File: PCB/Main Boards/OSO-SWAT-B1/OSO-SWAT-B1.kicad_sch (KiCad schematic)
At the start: 35 parts, among them J1 OSO_SWD, U1 ATSAML22J18A-MUT, U2 MIC5365-3.3YC5-TR, X1 32.768 kHz, 12.5 pF

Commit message: as sent to JLCPCB 10/12
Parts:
- C1: LCSC Part (none) -> C19702
- C2, C3, C4: LCSC Part (none) -> C14663
- C5, C6, C9: LCSC Part (none) -> C15849
- C7, C8: LCSC Part (none) -> C1555
- D1: LCSC Part (none) -> C2972951
- FID10, FID11, FID7, FID8, FID9: Field4 (none) -> ${REFERENCE}; now not fitted; now left out of the parts list
- J1, U$2: now left out of the parts list
- L1: LCSC Part (none) -> C139245
- LED0: LCSC Part (none) -> C5829791
- R1: value TBD -> 1K; LCSC Part (none) -> C21190
- R3: LCSC Part (none) -> C440252
- R4: LCSC Part (none) -> C95204
- R6: LCSC Part (none) -> C21190
- R7: LCSC Part (none) -> C22775
- RESET0, RESET1: LCSC Part (none) -> C5185477
- TP1, TP10, TP6, TP7, TP8, TP9: now not fitted; now left out of the parts list
- U1: LCSC Part (none) -> C618315
- U2: LCSC Part (none) -> C47945
- X1: Field4 (none) -> ${REFERENCE}; LCSC Part (none) -> C2613043

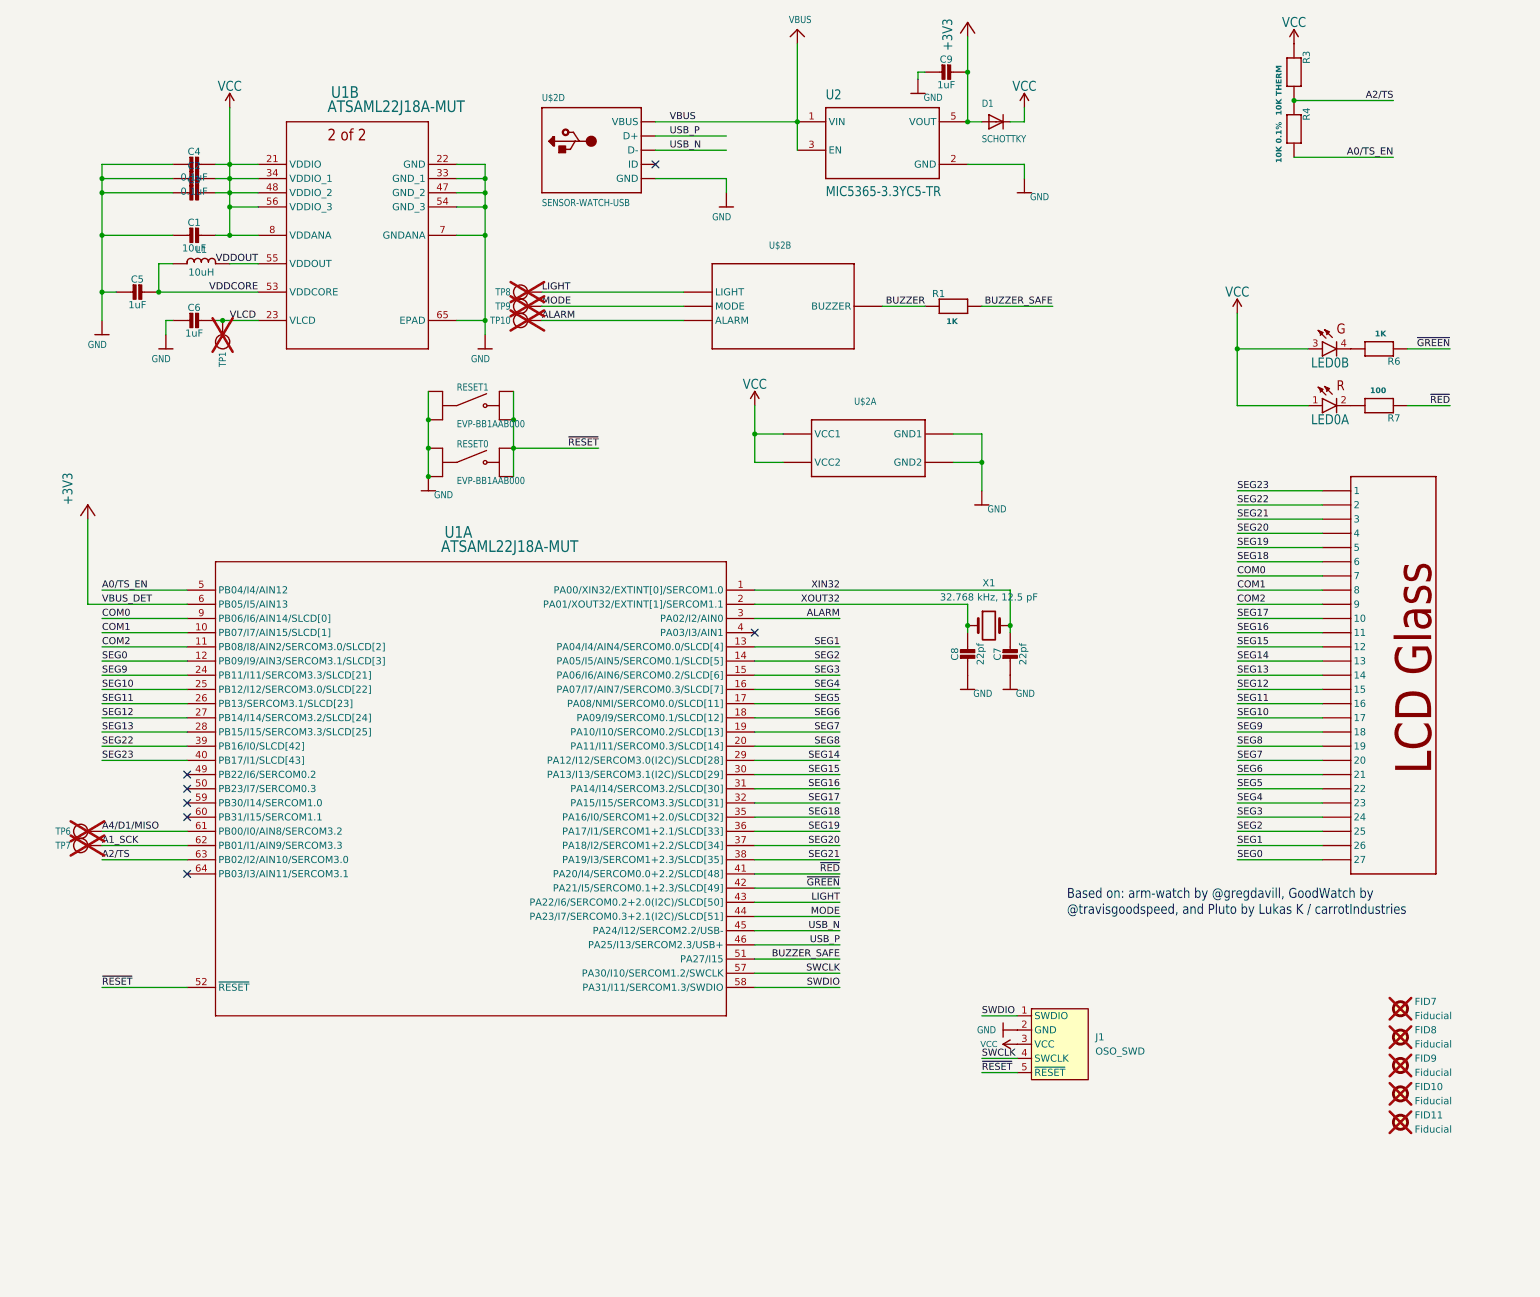
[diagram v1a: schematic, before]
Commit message: DFM changes for JLC release
- Change small value capacitors to 0.1uF
- Fix footprint / library associations
- Change test points to discrete footprints
- Use smaller LED
- Change to DFN-6 LDO
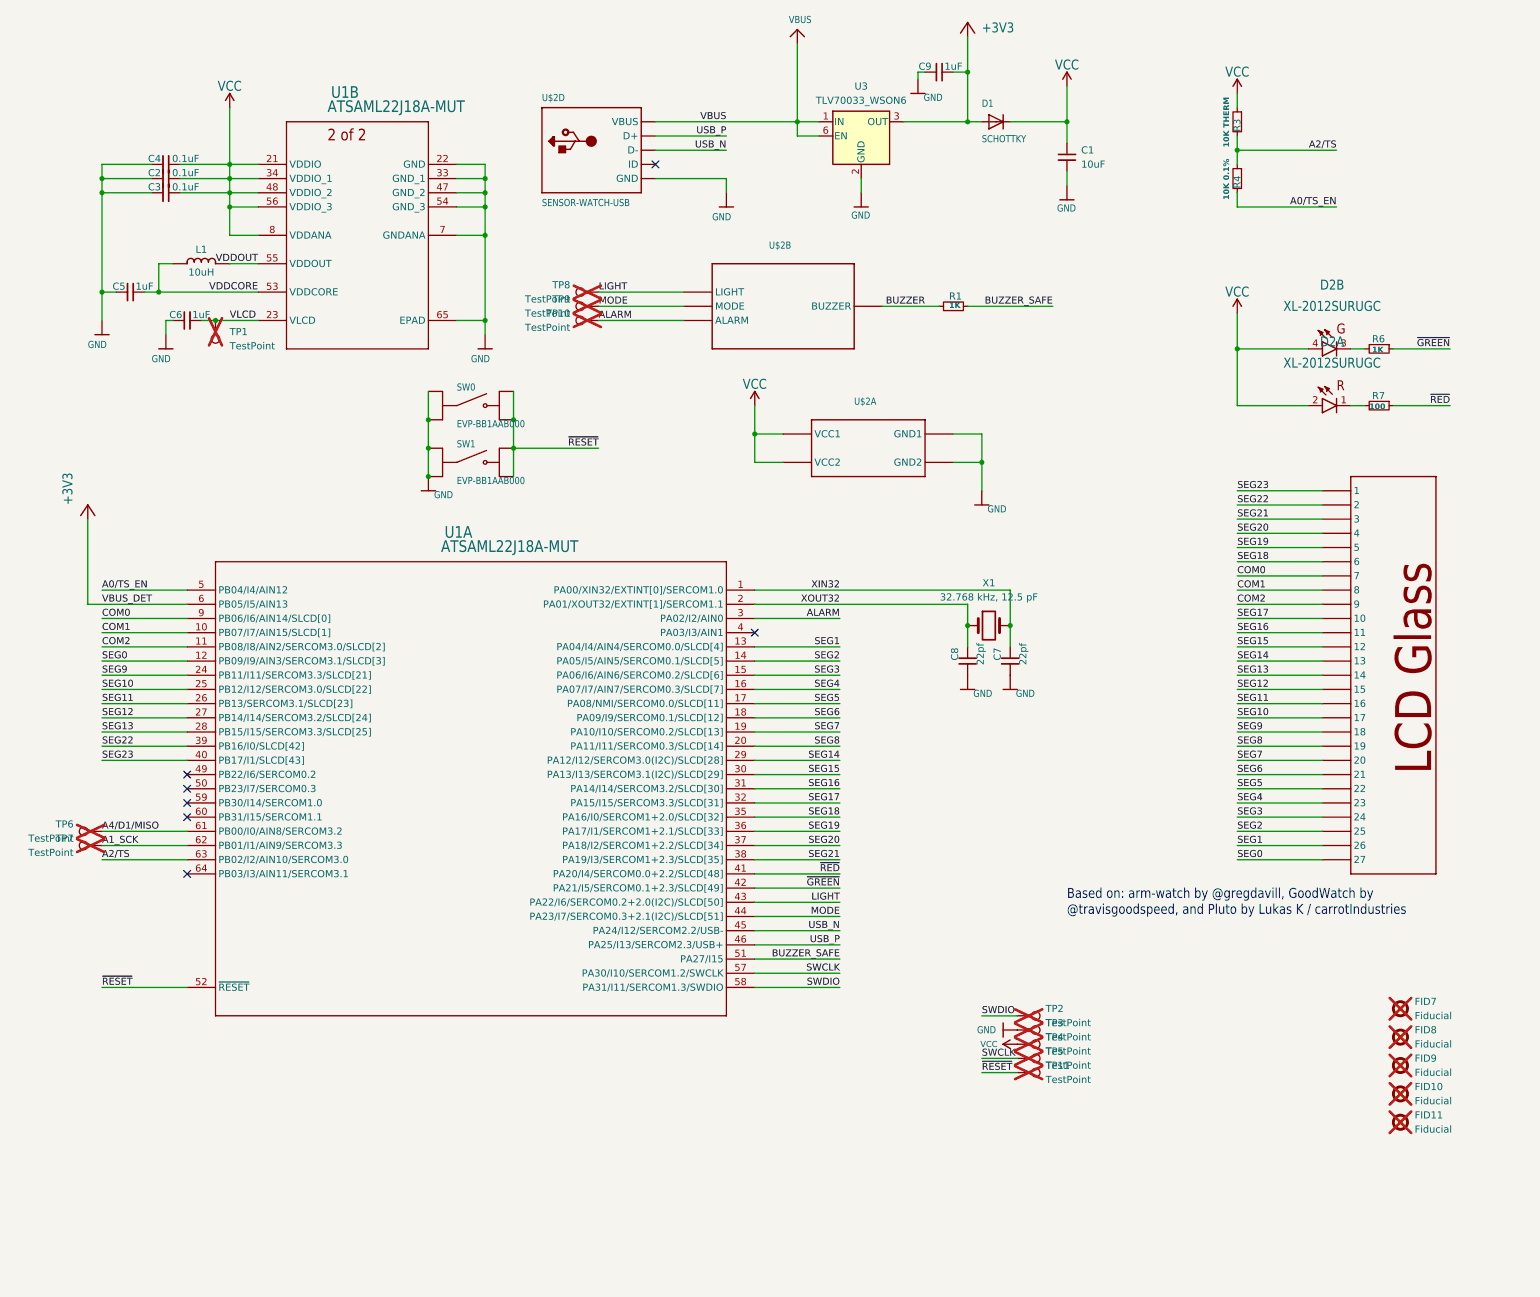
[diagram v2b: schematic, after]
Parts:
- removed J1: OSO_SWD, OSO-SWD:OSO_SWD_2x3, symbol OSO-SWD:OSO_SWD
- removed LED0: QBLP655-RIG, OSO-SWAT-A1-05:LED_QBLP655, symbol OSO-SWAT-A1-05-eagle-import:QBLP655-RIG
- removed TP1, TP10, TP6, TP7, TP8, TP9: MICROBUILDER_TESTPOINTROUND1.5MM, OSO-SWAT-A1-05:MICROBUILDER_TESTPOINT_ROUND_1.5MM, symbol OSO-SWAT-A1-05-eagle-import:MICROBUILDER_TESTPOINTROUND1.5MM
- removed U2: MIC5365-3.3YC5-TR, OSO-SWAT-A1-05:SOT65P210X110-5N, symbol OSO-SWAT-A1-05-eagle-import:MIC5365-3.3YC5-TR
- added D2: XL-2012SURUGC, OSO-SWAT-A1-05:LED-SMD_4P-L2.0-W1.3-RD-TL, symbol OSO-SWAT-A1-05-eagle-import:XL-2012SURUGC
- added TP1, TP10, TP11, TP2, TP3, TP4, TP5, TP6, TP7, TP8, TP9: TestPoint, TestPoint:TestPoint_Pad_D1.5mm, symbol Connector:TestPoint
- added U3: TLV70033_WSON6, Package_SON:WSON-6_1.5x1.5mm_P0.5mm, symbol Regulator_Linear:TLV70033_WSON6
- C1: symbol OSO-SWAT-A1-05-eagle-import:CAP_CERAMIC_0603MP -> Device:C_Small
- C2, C3, C4: footprint OSO-SWAT-A1-05:_0603MP -> OSO-SWAT-A1-05:_0402MP; symbol OSO-SWAT-A1-05-eagle-import:CAP_CERAMIC_0603MP -> Device:C_Small; LCSC Part C14663 -> C1525
- C5, C6, C9: footprint OSO-SWAT-A1-05:_0603MP -> OSO-SWAT-A1-05:_0402MP; symbol OSO-SWAT-A1-05-eagle-import:CAP_CERAMIC_0603MP -> Device:C_Small; LCSC Part C15849 -> C52923
- C7, C8: symbol OSO-SWAT-A1-05-eagle-import:CAP_CERAMIC_0402MP -> Device:C_Small
- R1, R3, R4: symbol OSO-SWAT-A1-05-eagle-import:RESISTOR_0603MP -> Device:R_Small
- R6: footprint OSO-SWAT-A1-05:_0603MP -> OSO-SWAT-A1-05:_0402MP; symbol OSO-SWAT-A1-05-eagle-import:RESISTOR_0603MP -> Device:R_Small; LCSC Part C21190 -> C11702
- R7: footprint OSO-SWAT-A1-05:_0603MP -> OSO-SWAT-A1-05:_0402MP; symbol OSO-SWAT-A1-05-eagle-import:RESISTOR_0603MP -> Device:R_Small; LCSC Part C22775 -> C25076
- renumbered RESET1 to SW0, RESET0 to SW1
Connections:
- net +3V3: now also U3.3 (OUT)
- net A1_SCK: now also TP7.1
- net A4/D1/MISO: now also TP6.1
- net ALARM: now also TP10.1
- net GND: now also TP3.1, U3.2 (GND)
- net LIGHT: now also TP8.1
- net MODE: now also TP9.1
- net SWCLK: now also TP5.1
- net SWDIO: now also TP2.1
- net VBUS: now also U3.1 (IN), U3.6 (EN)
- net VCC: now also D2.2 (A), D2.4 (A), TP4.1
- net VLCD: now also TP1.1
- net ~{RESET}: now also TP11.1
- net at R6.2: now also D2.3 (C)
- net at R7.2: now also D2.1 (C)
